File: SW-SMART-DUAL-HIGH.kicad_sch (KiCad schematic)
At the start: 42 parts, among them IC1 MCP1416, J1 SWLINK, J2 USART1, SW1 BTS50010-1TAD, SW2 VNB35N07xx-E, U1 STM32G0B1KBTx, U4 MCP2562-E-SN

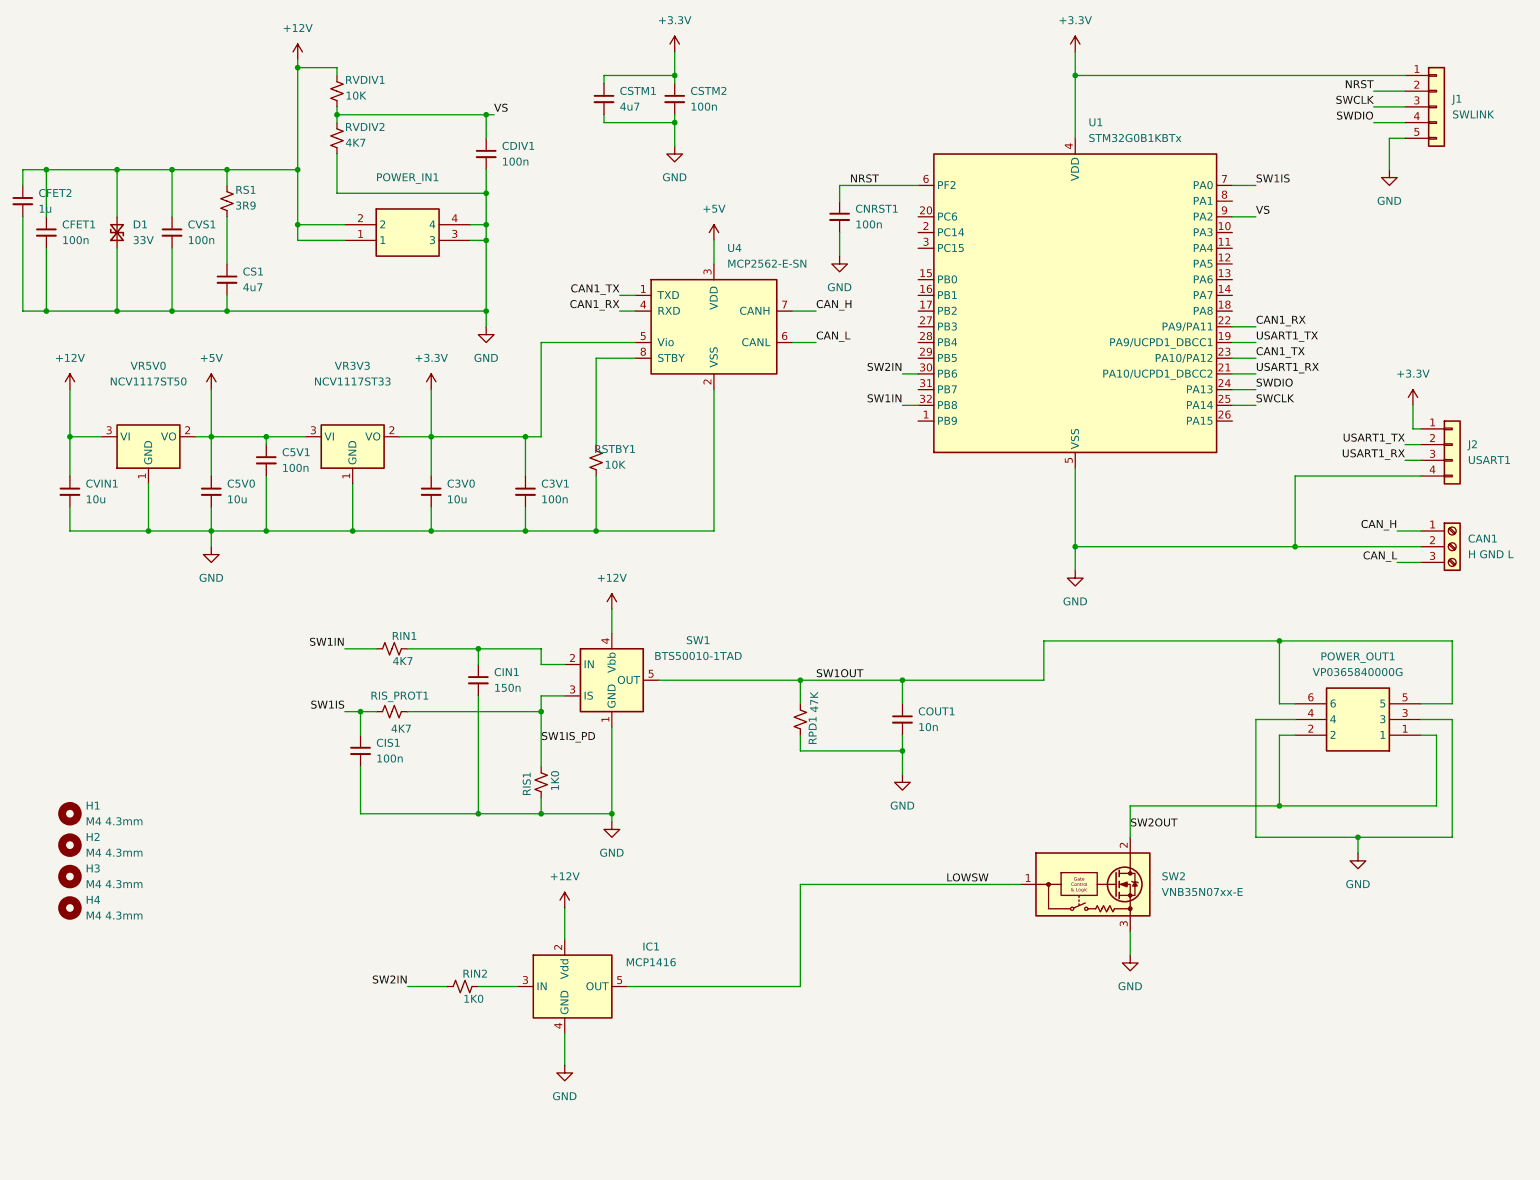
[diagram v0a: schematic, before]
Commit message: lots of rework to adapt previous layout to new switch configuration
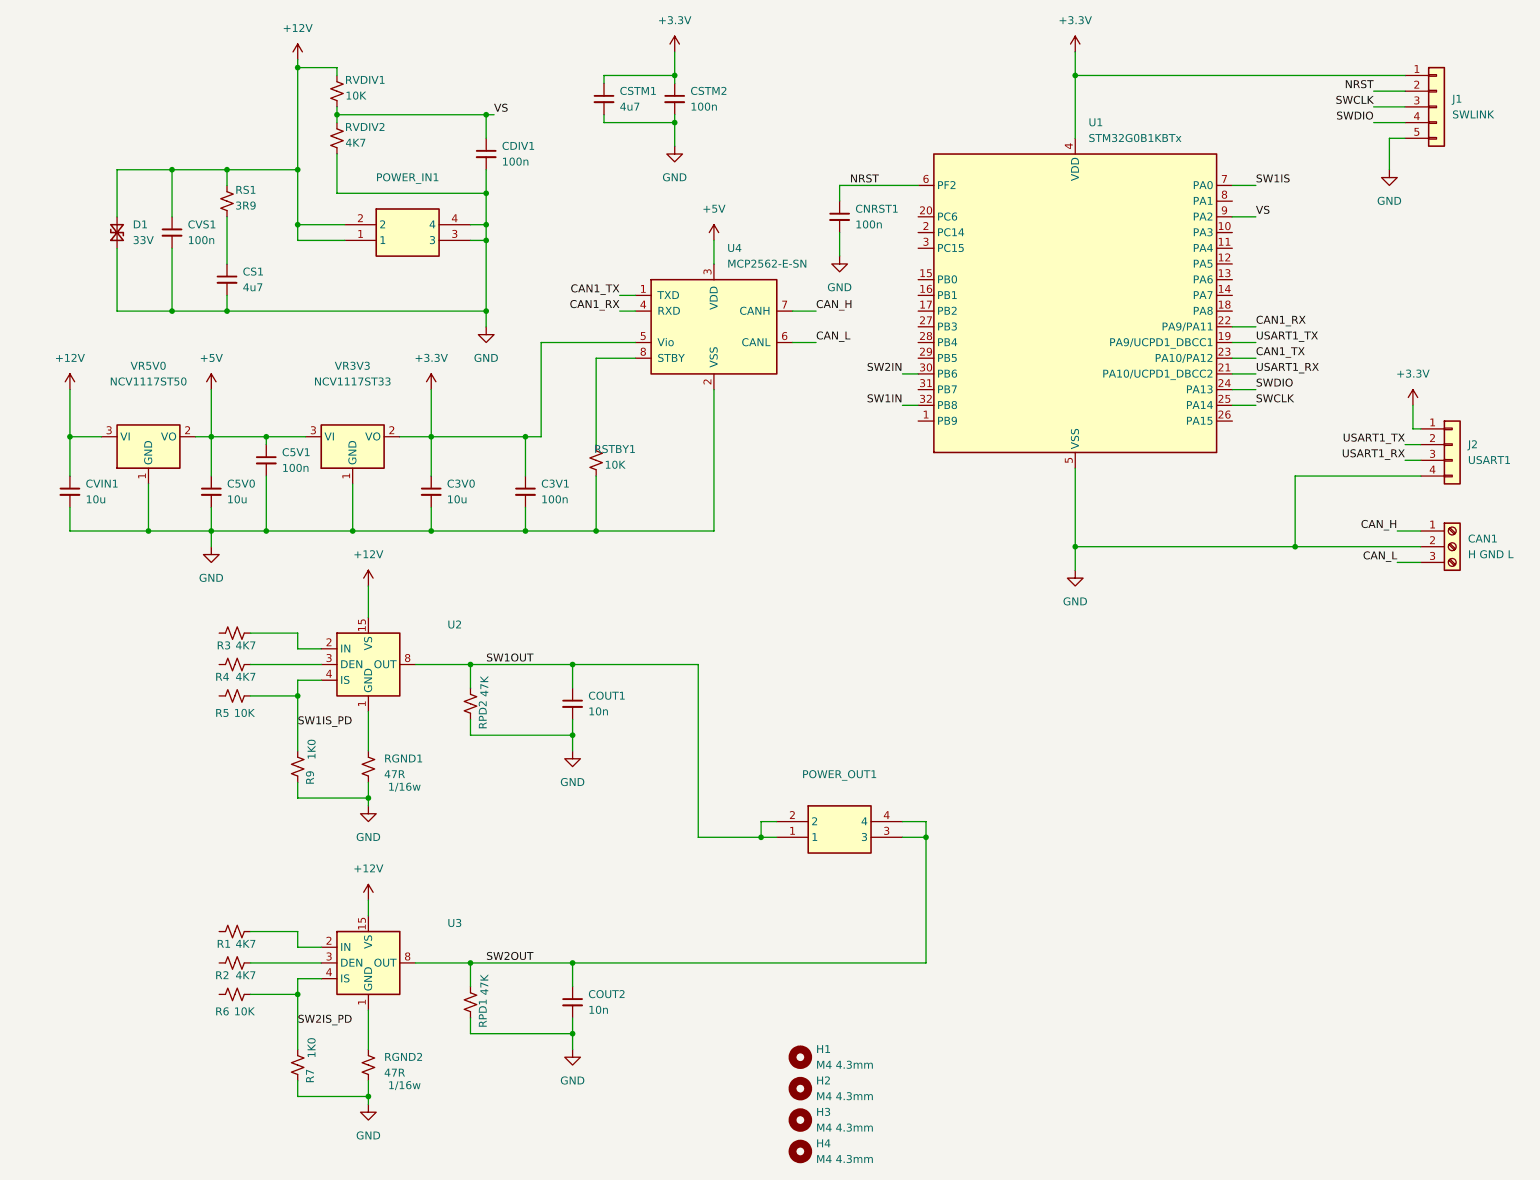
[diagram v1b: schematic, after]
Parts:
- removed CFET1, CIS1: 100n, Capacitor_SMD:C_0603_1608Metric_Pad1.08x0.95mm_HandSolder, symbol Device:C_Small
- removed CFET2: 1u, Capacitor_SMD:C_0805_2012Metric_Pad1.18x1.45mm_HandSolder, symbol Device:C_Small
- removed CIN1: 150n, Capacitor_SMD:C_0603_1608Metric_Pad1.08x0.95mm_HandSolder, symbol Device:C_Small
- removed IC1: MCP1416, Package_TO_SOT_SMD:SOT-23-5, symbol Driver_FET:MCP1416
- removed POWER_OUT1: VP0365840000G, VP0365840000G, symbol SamacSys_Parts:VP0365840000G
- removed RIN2: 1K0, Resistor_SMD:R_0603_1608Metric_Pad0.98x0.95mm_HandSolder, symbol Device:R_Small_US
- removed SW1: BTS50010-1TAD, Package_TO_SOT_SMD:TO-263-7_TabPin4, symbol Power_Management:BTS50010-1TAD
- removed SW2: VNB35N07xx-E, Package_TO_SOT_SMD:TO-263-2, symbol Transistor_FET_Other:VNB35N07xx-E
- added COUT2: 10n, Capacitor_SMD:C_0603_1608Metric_Pad1.08x0.95mm_HandSolder, symbol Device:C_Small
- added POWER_OUT1: SW1+ SW2+, VP0265840000G, symbol SamacSys_Parts:VP0265840000G
- added R1, R2, R4: 4K7, Resistor_SMD:R_0603_1608Metric_Pad0.98x0.95mm_HandSolder, symbol Device:R_Small_US
- added R6: 10K, Resistor_SMD:R_0603_1608Metric_Pad0.98x0.95mm_HandSolder, symbol Device:R_Small_US
- added R7: 1K0, Resistor_SMD:R_0603_1608Metric_Pad0.98x0.95mm_HandSolder, symbol Device:R_Small_US
- added RGND1, RGND2: 47R, Resistor_SMD:R_0603_1608Metric_Pad0.98x0.95mm_HandSolder, symbol Device:R_Small_US
- added RPD2: 47K, Resistor_SMD:R_0603_1608Metric_Pad0.98x0.95mm_HandSolder, symbol Device:R_Small_US
- added U2, U3: BTS7002-1EPP, SamacSys_Parts:SOP65P600X115-15N, symbol Power_Management:BTS7004-1EPP
- R5: renamed from RIS_PROT1; value 4K7 -> 10K
- renumbered RIN1 to R3, RIS1 to R9
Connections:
- net +12V: now also U2.15 (VS), U3.15 (VS)
- net GND: now also COUT2.2, R7.1, RGND1.2, RGND2.2, RPD2.1
- net SW1IN: no longer R3.1
- net SW1IS: no longer R5.1
- net SW1IS_PD: now also U2.4 (IS)
- net SW1OUT: now also POWER_OUT1.1, POWER_OUT1.2, RPD2.2, U2.10 (OUT), U2.12 (OUT), U2.13 (OUT), U2.14 (OUT), U2.8 (OUT), U2.9 (OUT); no longer RPD1.2
- net SW2OUT: now also RPD1.2, COUT2.1, POWER_OUT1.3, POWER_OUT1.4, U3.10 (OUT), U3.12 (OUT), U3.13 (OUT), U3.14 (OUT), U3.8 (OUT), U3.9 (OUT)
- net at R3.2: now also U2.2 (IN)
- new net: RGND2.1, U3.1 (GND)
- new net: R1.2, U3.2 (IN)
- new net: R2.2, U3.3 (DEN)
- new net: RGND1.1, U2.1 (GND)
- new net: R4.2, U2.3 (DEN)
- new net SW2IS_PD: R6.2, R7.2, U3.4 (IS)
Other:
- title: High / Low Smart Switch -> Smart Dual High Side Switch
- moved on the sheet: H1, H2, H3, H4, R3, R5, R9

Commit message: schematic tweaks
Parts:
- removed CVS1: 100n, Capacitor_SMD:C_0603_1608Metric_Pad1.08x0.95mm_HandSolder, symbol Device:C_Small
- removed POWER_OUT1: SW1+ SW2+, VP0265840000G, symbol SamacSys_Parts:VP0265840000G
- removed RS1: 3R9, Resistor_SMD:R_0603_1608Metric_Pad0.98x0.95mm_HandSolder, symbol Device:R_Small_US
- added CVS2: 68n, Capacitor_SMD:C_0603_1608Metric_Pad1.08x0.95mm_HandSolder, symbol Device:C_Small
- added POWER_OUT1: (no value), TerminalBlock_Phoenix:TerminalBlock_Phoenix_MKDS-1,5-3-5.08_1x03_P5.08mm_Horizontal, symbol Connector:Screw_Terminal_01x03
- CVS1: renamed from CS1; value 4u7 -> 68n
- RVDIV1: value 10K -> 4K7
- RVDIV2: value 4K7 -> 1K0
- renumbered U2 to SW1, U3 to SW2
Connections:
- net +12V: now also CVS1.1, CVS2.1
- net GND: now also CVS2.2
- net SW1IN: now also R3.1
- net SW1IS: now also R5.1
- net SW1OUT: now also POWER_OUT1.3 (Pin_3)
- net SW2IN: now also R1.1
- net SW2OUT: now also POWER_OUT1.1 (Pin_1)
- net SW2DEN: now reaches R2.1
- net SW2DEN: now also U1.29 (PB5)
- net SW2IS: now reaches R6.1
- net SW2IS: now also U1.8 (PA1)
- net SW1DEN: now reaches U1.31 (PB7)
- net SW1DEN: now also R4.1
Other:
- moved on the sheet: CVS1
